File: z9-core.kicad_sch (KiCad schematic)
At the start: 0 parts

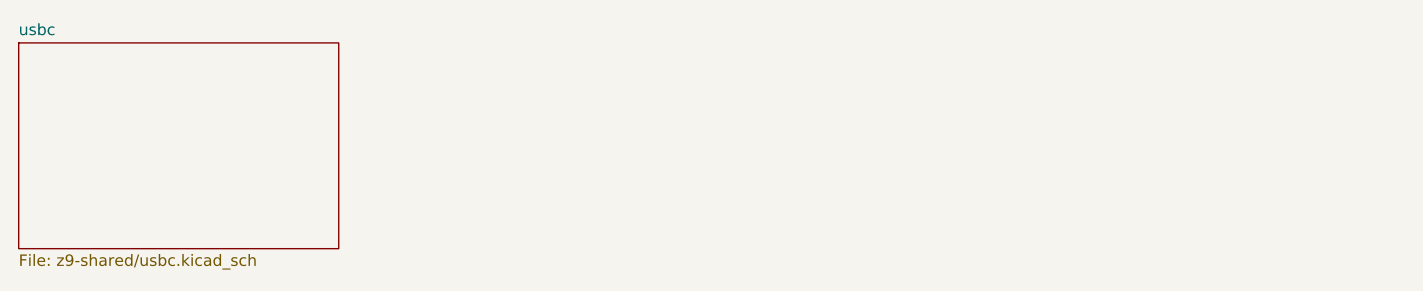
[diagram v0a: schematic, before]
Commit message: Core add KiCad library and schematic updates, including new components and ERC report
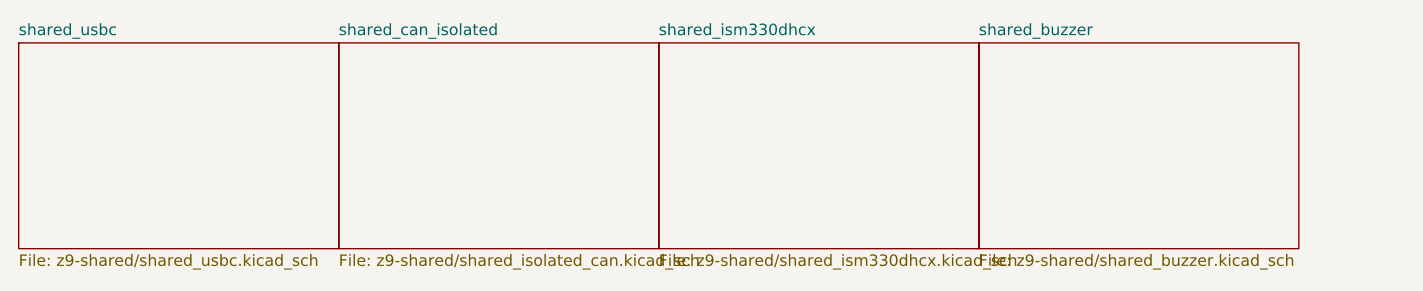
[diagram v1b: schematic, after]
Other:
- sheet usbc renamed shared_usbc
- added sheet shared_buzzer (z9-shared/shared_buzzer.kicad_sch)
- added sheet shared_can_isolated (z9-shared/shared_isolated_can.kicad_sch)
- added sheet shared_ism330dhcx (z9-shared/shared_ism330dhcx.kicad_sch)
- sheet shared_usbc: file z9-shared/usbc.kicad_sch -> z9-shared/shared_usbc.kicad_sch
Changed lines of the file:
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@@
 (kicad_sch
-	(version 20250114)
+	(version 20260306)
 	(generator "eeschema")
-	(generator_version "9.0")
+	(generator_version "10.0")
 	(paper "A4")
 	(sheet
@@
 			(color 0 0 0 0.0000)
 		)
-		(property "Sheetname" "usbc"
+		(property "Sheetname" "shared_usbc"
 			(at 44.45 32.3084 0)
 			(effects
@@
 			)
 		)
-		(property "Sheetfile" "z9-shared/usbc.kicad_sch"
+		(property "Sheetfile" "z9-shared/shared_usbc.kicad_sch"
 			(at 44.45 56.4646 0)
 			(effects
@@
 				)
 			)
+		)
+	)
+	(sheet
+		(at 80.01 33.02)
+		(size 35.56 22.86)
+		(exclude_from_sim no)
+		(in_bom yes)
+		(on_board yes)
+		(dnp no)
+		(fields_autoplaced yes)
+		(stroke
+			(width 0.1524)
+			(type solid)
+		)
+		(fill
+			(color 0 0 0 0.0000)
+		)
+		(property "Sheetname" "shared_can_isolated"
+			(at 80.01 32.3084 0)
+			(effects
+				(font
+					(size 1.27 1.27)
+				)
+				(justify left bottom)
+			)
+		)
+		(property "Sheetfile" "z9-shared/shared_isolated_can.kicad_sch"
+			(at 80.01 56.4646 0)
+			(effects
+				(font
+					(size 1.27 1.27)
+				)
+				(justify left top)
+			)
+		)
+		(instances
+			(project "z9-core"
+				(path "/392ab61e-cb83-4945-9e87-ff2a5807a99d"
+					(page "3")
+				)
+			)
+		)
+	)
+	(sheet
+		(at 115.57 33.02)
+		(size 35.56 22.86)
+		(exclude_from_sim no)
+		(in_bom yes)
+		(on_board yes)
+		(dnp no)
+		(fields_autoplaced yes)
+		(stroke
+			(width 0.1524)
+			(type solid)
+		)
+		(fill
+			(color 0 0 0 0.0000)
+		)
+		(property "Sheetname" "shared_ism330dhcx"
+			(at 115.57 32.3084 0)
+			(effects
+				(font
+					(size 1.27 1.27)
+				)
+				(justify left bottom)
+			)
+		)
+		(property "Sheetfile" "z9-shared/shared_ism330dhcx.kicad_sch"
+			(at 115.57 56.4646 0)
+			(effects
+				(font
+					(size 1.27 1.27)
+				)
+				(justify left top)
+			)
+		)
+		(instances
+			(project "z9-core"
+				(path "/392ab61e-cb83-4945-9e87-ff2a5807a99d"
+					(page "4")
+				)
+			)
+		)
+	)
+	(sheet
+		(at 151.13 33.02)
+		(size 35.56 22.86)
+		(exclude_from_sim no)
+		(in_bom yes)
+		(on_board yes)
+		(dnp no)
+		(fields_autoplaced yes)
+		(stroke
+			(width 0.1524)
+			(type solid)
+		)
+		(fill
+			(color 0 0 0 0.0000)
+		)
+		(property "Sheetname" "shared_buzzer"
+			(at 151.13 32.3084 0)
+			(effects
+				(font
+					(size 1.27 1.27)
+				)
+				(justify left bottom)
+			)
+		)
+		(property "Sheetfile" "z9-shared/shared_buzzer.kicad_sch"
+			(at 151.13 56.4646 0)
+			(effects
+				(font
+					(size 1.27 1.27)
+				)
+				(justify left top)
+			)
+		)
+		(instances
+			(project "z9-core"
+				(path "/392ab61e-cb83-4945-9e87-ff2a5807a99d"
+					(page "5")
+				)
+			)
